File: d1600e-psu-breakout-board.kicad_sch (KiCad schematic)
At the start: 60 parts, among them J10 10107844-002LF, J2 BM04B-SRSS-TB-LF-SN, J3 BM04B-SRSS-TB-LF-SN, J4 39288080, J5 39288080, J6 39288080, J7 39288080, J8 39288080, Q11 BC856,215

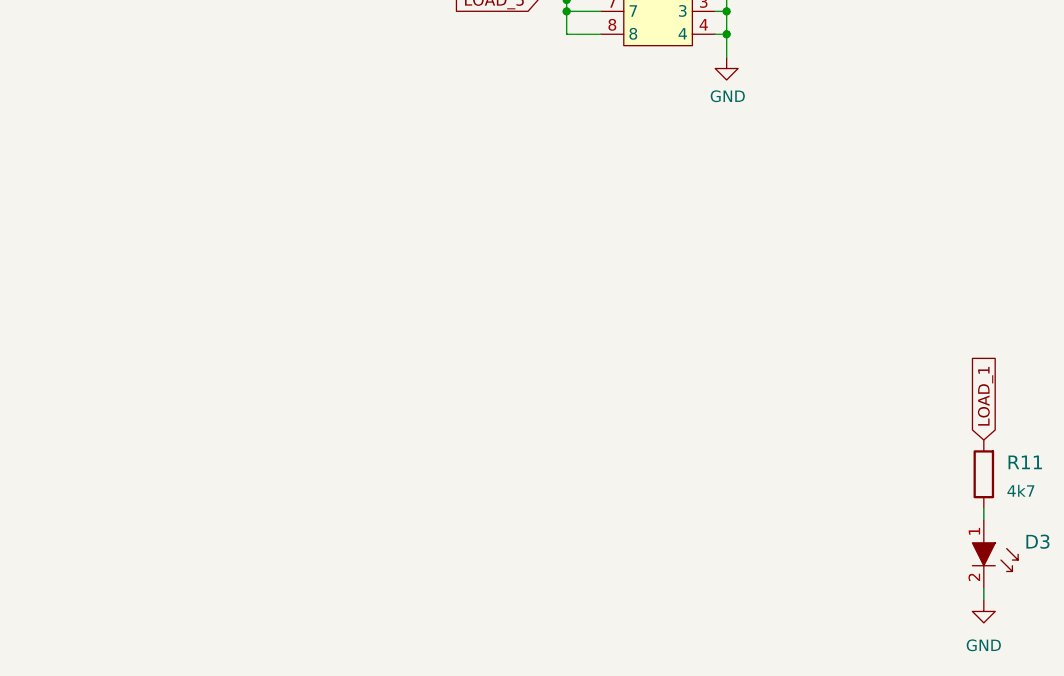
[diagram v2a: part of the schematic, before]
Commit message: Aded molex connectors for PCI-e risers and pul up down option for 5V info rail from coordinator
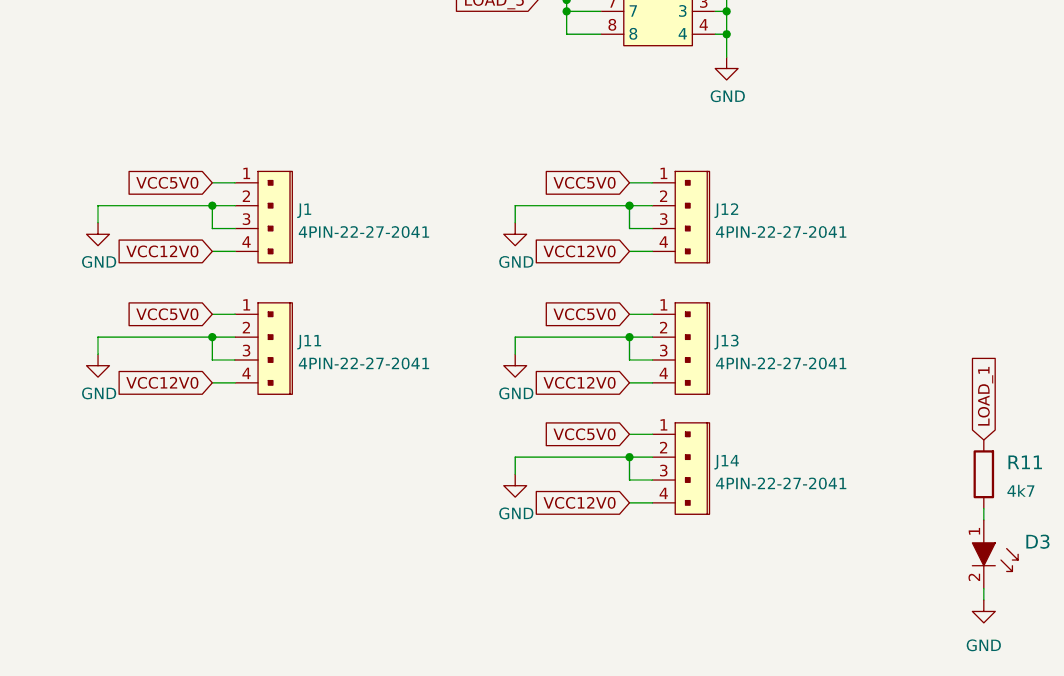
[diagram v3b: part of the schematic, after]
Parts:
- added J1, J11, J12, J13, J14: 4PIN-22-27-2041, antmicro-footprints:4PIN-22-27-2041, symbol antmicroRectangularConnectorsHeadersMalePins:4PIN-22-27-2041
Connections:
- net GND: now also J1.2, J1.3, J11.2, J11.3, J12.2, J12.3, J13.2, J13.3, J14.2, J14.3
- net P3/4: now also J1.4, J11.4, J12.4, J13.4, J14.4
- net VCC5V0: now also J1.1, J11.1, J12.1, J13.1, J14.1

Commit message: Added some changes after 1st review
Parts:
- added D12, D13: PESD5V0S2BQA, d1600e-psu-breakout-board-footprints:TPD2E009DRTR, symbol d1600e-psu-breakout-board:PESD5V0S2BQA
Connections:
- net GND: now also D12.3 (GND), D13.3 (GND)
- net SCL: now also D12.1 (IO1), D13.1 (IO1)
- net SDA: now also D12.2 (IO2), D13.2 (IO2)
